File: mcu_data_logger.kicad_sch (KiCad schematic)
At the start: 0 parts

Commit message: second commit, dropped in components
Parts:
- added BT1: Battery, symbol Device:Battery
- added C1, C2, C3, C4: C, symbol Device:C
- added C5: C_Polarized, symbol Device:C_Polarized
- added D1, D2: LED, symbol Device:LED
- added H1, H2, H3, H4: MountingHole, symbol Mechanical:MountingHole
- added R1, R2, R3, R4, R5, R6, R7: R, symbol Device:R
- added U1, U2: 24LC1025, symbol Memory_EEPROM:24LC1025
- added U3: DS1337S_, DS1337S_:SOIC127P600X175-8N, symbol DS1337S_:DS1337S_
- added U4: ATMEGA328P-AU, ATMEGA328P-AU:QFP80P900X900X120-32N, symbol ATMEGA328P-AU:ATMEGA328P-AU
- added Y1, Y2: Crystal, symbol Device:Crystal
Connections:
- new net: U4.21 (GND), U4.3 (GND), U4.5 (GND)
- new net: U4.4 (VCC), U4.6 (VCC)

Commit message: arranged symbols on the schematic
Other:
- added sheet Connectors (connectors.kicad_sch)
- moved on the sheet: BT1, C1, C2, C3, C4, C5, D1, D2, R1, R2, R3, R4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

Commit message: assigned values to components
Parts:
- C1, C4: value C -> 0.1uF
- C2, C3: value C -> 22pF
- C5: value C_Polarized -> 100nF
- R1, R2, R6: value R -> 10k
- R3, R4: value R -> 4.7k
- R5, R7: value R -> 330
- Y1: value Crystal -> 32.768 kHz
- Y2: value Crystal -> 16MHz
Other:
- moved on the sheet: R7
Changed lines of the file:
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@@
 			)
 		)
-		(property "Value" "C"
+		(property "Value" "0.1uF"
 			(at 189.23 24.13 90)
 			(effects
@@
 			)
 		)
+		(property "Purpose" ""
+			(at 189.23 29.21 0)
+			(effects
+				(font
+					(size 1.27 1.27)
+				)
+			)
+		)
 		(pin "1"
 		)
@@
 			)
 		)
-		(property "Value" "C"
+		(property "Value" "0.1uF"
 			(at 134.62 52.0699 0)
 			(effects
@@
 			)
 		)
+		(property "Purpose" ""
+			(at 130.81 50.8 0)
+			(effects
+				(font
+					(size 1.27 1.27)
+				)
+			)
+		)
 		(pin "1"
 		)
@@
 			)
 		)
-		(property "Value" "C"
+		(property "Value" "22pF"
 			(at 177.8 77.4699 0)
 			(effects
@@
 			)
 		)
+		(property "Purpose" ""
+			(at 173.99 76.2 0)
+			(effects
+				(font
+					(size 1.27 1.27)
+				)
+			)
+		)
 		(pin "1"
 		)
@@
 			)
 		)
-		(property "Value" "C_Polarized"
+		(property "Value" "100nF"
 			(at 257.81 44.8309 0)
 			(effects
@@
 			)
 		)
+		(property "Purpose" ""
+			(at 254 44.45 0)
+			(effects
+				(font
+					(size 1.27 1.27)
+				)
+			)
+		)
 		(pin "1"
 		)
@@
 	(symbol
 		(lib_id "Device:R")
-		(at 256.54 82.55 0)
+		(at 254 76.2 0)
 		(unit 1)
 		(exclude_from_sim no)
@@
 		(fields_autoplaced yes)
 		(property "Reference" "R7"
-			(at 259.08 81.2799 0)
-			(effects
-				(font
-					(size 1.27 1.27)
-				)
-				(justify left)
-			)
-		)
-		(property "Value" "R"
-			(at 259.08 83.8199 0)
-			(effects
-				(font
-					(size 1.27 1.27)
-				)
-				(justify left)
-			)
-		)
-		(property "Footprint" ""
-			(at 254.762 82.55 90)
+			(at 256.54 74.9299 0)
+			(effects
+				(font
+					(size 1.27 1.27)
+				)
+				(justify left)
+			)
+		)
+		(property "Value" "330"
+			(at 256.54 77.4699 0)
+			(effects
+				(font
+					(size 1.27 1.27)
+				)
+				(justify left)
+			)
+		)
+		(property "Footprint" ""
+			(at 252.222 76.2 90)
 			(effects
 				(font
@@
 		)
 		(property "Datasheet" "~"
-			(at 256.54 82.55 0)
+			(at 254 76.2 0)
 			(effects
 				(font
@@
 		)
 		(property "Description" "Resistor"
-			(at 256.54 82.55 0)
-			(effects
-				(font
-					(size 1.27 1.27)
-				)
-				(hide yes)
+			(at 254 76.2 0)
+			(effects
+				(font
+					(size 1.27 1.27)
+				)
+				(hide yes)
+			)
+		)
+		(property "Purpose" ""
+			(at 254 76.2 0)
+			(effects
+				(font
+					(size 1.27 1.27)
+				)
 			)
 		)
@@
 				(path "/8d241645-05dd-4180-8806-a9efe0716d11"
 					(reference "R7")
+					(unit 1)
+				)
+			)
+		)
+	)
+	(symbol
+		(lib_id "Device:R")
+		(at 130.81 172.72 0)
+		(unit 1)
+		(exclude_from_sim no)
+		(in_bom yes)
+		(on_board yes)
+		(dnp no)
+		(fields_autoplaced yes)
+		(property "Reference" "R3"
+			(at 133.35 171.4499 0)
+			(effects
+				(font
+					(size 1.27 1.27)
+				)
+				(justify left)
+			)
+		)
+		(property "Value" "4.7k"
+			(at 133.35 173.9899 0)
+			(effects
+				(font
+					(size 1.27 1.27)
+				)
+				(justify left)
+			)
+		)
+		(property "Footprint" ""
+			(at 129.032 172.72 90)
+			(effects
+				(font
+					(size 1.27 1.27)
+				)
+				(hide yes)
+			)
+		)
+		(property "Datasheet" "~"
+			(at 130.81 172.72 0)
+			(effects
+				(font
+					(size 1.27 1.27)
+				)
+				(hide yes)
+			)
+		)
+		(property "Description" "Resistor"
+			(at 130.81 172.72 0)
+			(effects
+				(font
+					(size 1.27 1.27)
+				)
+				(hide yes)
+			)
+		)
+		(property "Purpose" ""
+			(at 130.81 172.72 0)
+			(effects
+				(font
+					(size 1.27 1.27)
+				)
+			)
+		)
+		(pin "1"
+		)
+		(pin "2"
+		)
+		(instances
+			(project "mcu_data_logger"
+				(path "/8d241645-05dd-4180-8806-a9efe0716d11"
+					(reference "R3")
 					(unit 1)
 				)
@@
 			)
 		)
-		(property "Value" "R"
+		(property "Value" "10k"
 			(at 109.22 52.0699 0)
 			(effects
@@
 			)
 		)
+		(property "Purpose" ""
+			(at 106.68 50.8 0)
+			(effects
+				(font
+					(size 1.27 1.27)
+				)
+			)
+		)
 		(pin "1"
 		)
@@
 			)
 		)
-		(property "Value" "R"
+		(property "Value" "330"
 			(at 173.99 41.91 90)
 			(effects
@@
 			)
 		)
+		(property "Purpose" ""
+			(at 173.99 45.72 0)
+			(effects
+				(font
+					(size 1.27 1.27)
+				)
+			)
+		)
 		(pin "1"
 		)
@@
 			)
 		)
-		(property "Value" "R"
+		(property "Value" "10k"
 			(at 120.65 52.0699 0)
 			(effects
@@
 			)
 		)
+		(property "Purpose" ""
+			(at 118.11 50.8 0)
+			(effects
+				(font
+					(size 1.27 1.27)
+				)
+			)
+		)
 		(pin "1"
 		)
@@
 			)
 		)
-		(property "Value" "Crystal"
+		(property "Value" "32.768 kHz"
 			(at 48.26 52.0699 90)
 			(effects
@@
 			)
 		)
-		(property "Value" "C"
+		(property "Value" "22pF"
 			(at 177.8 59.6899 0)
 			(effects
@@
 			)
 		)
+		(property "Purpose" ""
+			(at 173.99 58.42 0)
+			(effects
+				(font
+					(size 1.27 1.27)
+				)
+			)
+		)
 		(pin "1"
 		)
@@
 				(path "/8d241645-05dd-4180-8806-a9efe0716d11"
 					(reference "C2")
-					(unit 1)
-				)
-			)
-		)
-	)
-	(symbol
-		(lib_id "Device:R")
-		(at 132.08 172.72 180)
-		(unit 1)
-		(exclude_from_sim no)
-		(in_bom yes)
-		(on_board yes)
-		(dnp no)
-		(fields_autoplaced yes)
-		(property "Reference" "R3"
-			(at 134.62 171.4499 0)
-			(effects
-				(font
-					(size 1.27 1.27)
-				)
-				(justify right)
-			)
-		)
-		(property "Value" "R"
-			(at 134.62 173.9899 0)
-			(effects
-				(font
-					(size 1.27 1.27)
-				)
-				(justify right)
-			)
-		)
-		(property "Footprint" ""
-			(at 133.858 172.72 90)
-			(effects
-				(font
-					(size 1.27 1.27)
-				)
-				(hide yes)
-			)
-		)
-		(property "Datasheet" "~"
-			(at 132.08 172.72 0)
-			(effects
-				(font
-					(size 1.27 1.27)
-				)
-				(hide yes)
-			)
-		)
-		(property "Description" "Resistor"
-			(at 132.08 172.72 0)
-			(effects
-				(font
-					(size 1.27 1.27)
-				)
-				(hide yes)
-			)
-		)
-		(pin "1"
-		)
-		(pin "2"
-		)
-		(instances
-			(project "mcu_data_logger"
-				(path "/8d241645-05dd-4180-8806-a9efe0716d11"
-					(reference "R3")
 					(unit 1)
 				)
@@
 			)
 		)
-		(property "Value" "R"
+		(property "Value" "10k"
 			(at 198.12 81.28 90)
 			(effects
@@
 			)
 		)
+		(property "Purpose" ""
+			(at 198.12 85.09 0)
+			(effects
+				(font
+					(size 1.27 1.27)
+				)
+			)
+		)
 		(pin "1"
 		)
@@
 			)
 		)
-		(property "Value" "Crystal"
+		(property "Value" "16MHz"
 			(at 194.31 63.4999 90)
 			(effects
@@
 			)
 		)
+		(property "Purpose" ""
+			(at 190.5 62.23 0)
+			(effects
+				(font
+					(size 1.27 1.27)
+				)
+			)
+		)
 		(pin "2"
 		)
@@
 			)
 		)
-		(property "Value" "R"
+		(property "Value" "4.7k"
 			(at 143.51 173.9899 0)
 			(effects
@@
 			)
 		)
+		(property "Purpose" ""
+			(at 140.97 172.72 0)
+			(effects
+				(font
+					(size 1.27 1.27)
+				)
+			)
+		)

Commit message: assigned footprints and added libraries
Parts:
- BT1: footprint (none) -> Connector_PinHeader_2.54mm:PinHeader_1x02_P2.54mm_Horizontal
- C1, C2, C3, C4, C5: footprint (none) -> Capacitor_SMD:C_0805_2012Metric
- D1, D2: footprint (none) -> LED_SMD:LED_0805_2012Metric
- H1, H2, H3, H4: footprint (none) -> MountingHole:MountingHole_2.1mm
- R1, R2, R3, R4, R5, R6, R7: footprint (none) -> Resistor_SMD:R_0805_2012Metric
- U1, U2: footprint (none) -> Package_SO:SOIC-8_5.3x5.3mm_P1.27mm
- U3: footprint DS1337S_:SOIC127P600X175-8N -> footprints:SOIC127P600X175-8N
- U4: footprint ATMEGA328P-AU:QFP80P900X900X120-32N -> footprints:QFP80P900X900X120-32N
- Y1, Y2: footprint (none) -> Crystal:Crystal_SMD_5032-2Pin_5.0x3.2mm_HandSoldering
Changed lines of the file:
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@@
 			)
 		)
-		(property "Footprint" ""
+		(property "Footprint" "Capacitor_SMD:C_0805_2012Metric"
 			(at 193.04 28.2448 0)
 			(effects
@@
 			)
 		)
-		(property "Footprint" ""
+		(property "Footprint" "Capacitor_SMD:C_0805_2012Metric"
 			(at 131.7752 54.61 0)
 			(effects
@@
 			)
 		)
-		(property "Footprint" ""
+		(property "Footprint" "Capacitor_SMD:C_0805_2012Metric"
 			(at 174.9552 80.01 0)
 			(effects
@@
 			)
 		)
-		(property "Footprint" ""
+		(property "Footprint" "Capacitor_SMD:C_0805_2012Metric"
 			(at 254.9652 48.26 0)
 			(effects
@@
 			)
 		)
-		(property "Footprint" ""
+		(property "Footprint" "Connector_PinHeader_2.54mm:PinHeader_1x02_P2.54mm_Horizontal"
 			(at 267.97 42.926 90)
 			(effects
@@
 			)
 		)
-		(property "Footprint" ""
+		(property "Footprint" "MountingHole:MountingHole_2.1mm"
 			(at 200.66 151.13 0)
 			(effects
@@
 			)
 		)
-		(property "Footprint" ""
+		(property "Footprint" "Package_SO:SOIC-8_5.3x5.3mm_P1.27mm"
 			(at 110.49 172.72 0)
 			(effects
@@
 			)
 		)
-		(property "Footprint" ""
+		(property "Footprint" "Package_SO:SOIC-8_5.3x5.3mm_P1.27mm"
 			(at 80.01 172.72 0)
 			(effects
@@
 			)
 		)
-		(property "Footprint" ""
+		(property "Footprint" "Resistor_SMD:R_0805_2012Metric"
 			(at 252.222 76.2 90)
 			(effects
@@
 			)
 		)
-		(property "Footprint" ""
+		(property "Footprint" "Resistor_SMD:R_0805_2012Metric"
 			(at 129.032 172.72 90)
 			(effects
@@
 			)
 		)
-		(property "Footprint" ""
+		(property "Footprint" "LED_SMD:LED_0805_2012Metric"
 			(at 189.23 45.72 0)
 			(effects
@@
 			)
 		)
-		(property "Footprint" ""
+		(property "Footprint" "Resistor_SMD:R_0805_2012Metric"
 			(at 104.902 50.8 90)
 			(effects
@@
 			)
 		)
-		(property "Footprint" ""
+		(property "Footprint" "MountingHole:MountingHole_2.1mm"
 			(at 200.66 140.97 0)
 			(effects
@@
 			)
 		)
-		(property "Footprint" ""
+		(property "Footprint" "Resistor_SMD:R_0805_2012Metric"
 			(at 173.99 47.498 90)
 			(effects
@@
 			)
 		)
-		(property "Footprint" ""
+		(property "Footprint" "Resistor_SMD:R_0805_2012Metric"
 			(at 116.332 50.8 90)
 			(effects
@@
 			)
 		)
-		(property "Footprint" "DS1337S_:SOIC127P600X175-8N"
+		(property "Footprint" "footprints:SOIC127P600X175-8N"
 			(at 73.66 53.34 0)
 			(effects
@@
 			)
 		)
-		(property "Footprint" ""
+		(property "Footprint" "Crystal:Crystal_SMD_5032-2Pin_5.0x3.2mm_HandSoldering"
 			(at 44.45 50.8 0)
 			(effects
@@
 			)
 		)
-		(property "Footprint" ""
+		(property "Footprint" "LED_SMD:LED_0805_2012Metric"
 			(at 254 62.23 0)
 			(effects
@@
 			)
 		)
-		(property "Footprint" ""
+		(property "Footprint" "Capacitor_SMD:C_0805_2012Metric"
 			(at 174.9552 62.23 0)
 			(effects
@@
 			)
 		)
-		(property "Footprint" ""
+		(property "Footprint" "Resistor_SMD:R_0805_2012Metric"
 			(at 198.12 86.868 90)
 			(effects
@@
 			)
 		)
-		(property "Footprint" ""
+		(property "Footprint" "MountingHole:MountingHole_2.1mm"
 			(at 200.66 128.27 0)
 			(effects
@@
 			)
 		)
-		(property "Footprint" "ATMEGA328P-AU:QFP80P900X900X120-32N"
+		(property "Footprint" "footprints:QFP80P900X900X120-32N"
 			(at 227.33 60.96 0)
 			(effects
@@
 			)
 		)
-		(property "Footprint" ""
+		(property "Footprint" "MountingHole:MountingHole_2.1mm"
 			(at 200.66 119.38 0)
 			(effects
@@
 			)
 		)
-		(property "Footprint" ""
+		(property "Footprint" "Crystal:Crystal_SMD_5032-2Pin_5.0x3.2mm_HandSoldering"
 			(at 190.5 62.23 0)
 			(effects
@@
 			)
 		)
-		(property "Footprint" ""
+		(property "Footprint" "Resistor_SMD:R_0805_2012Metric"
 			(at 139.192 172.72 90)
 			(effects

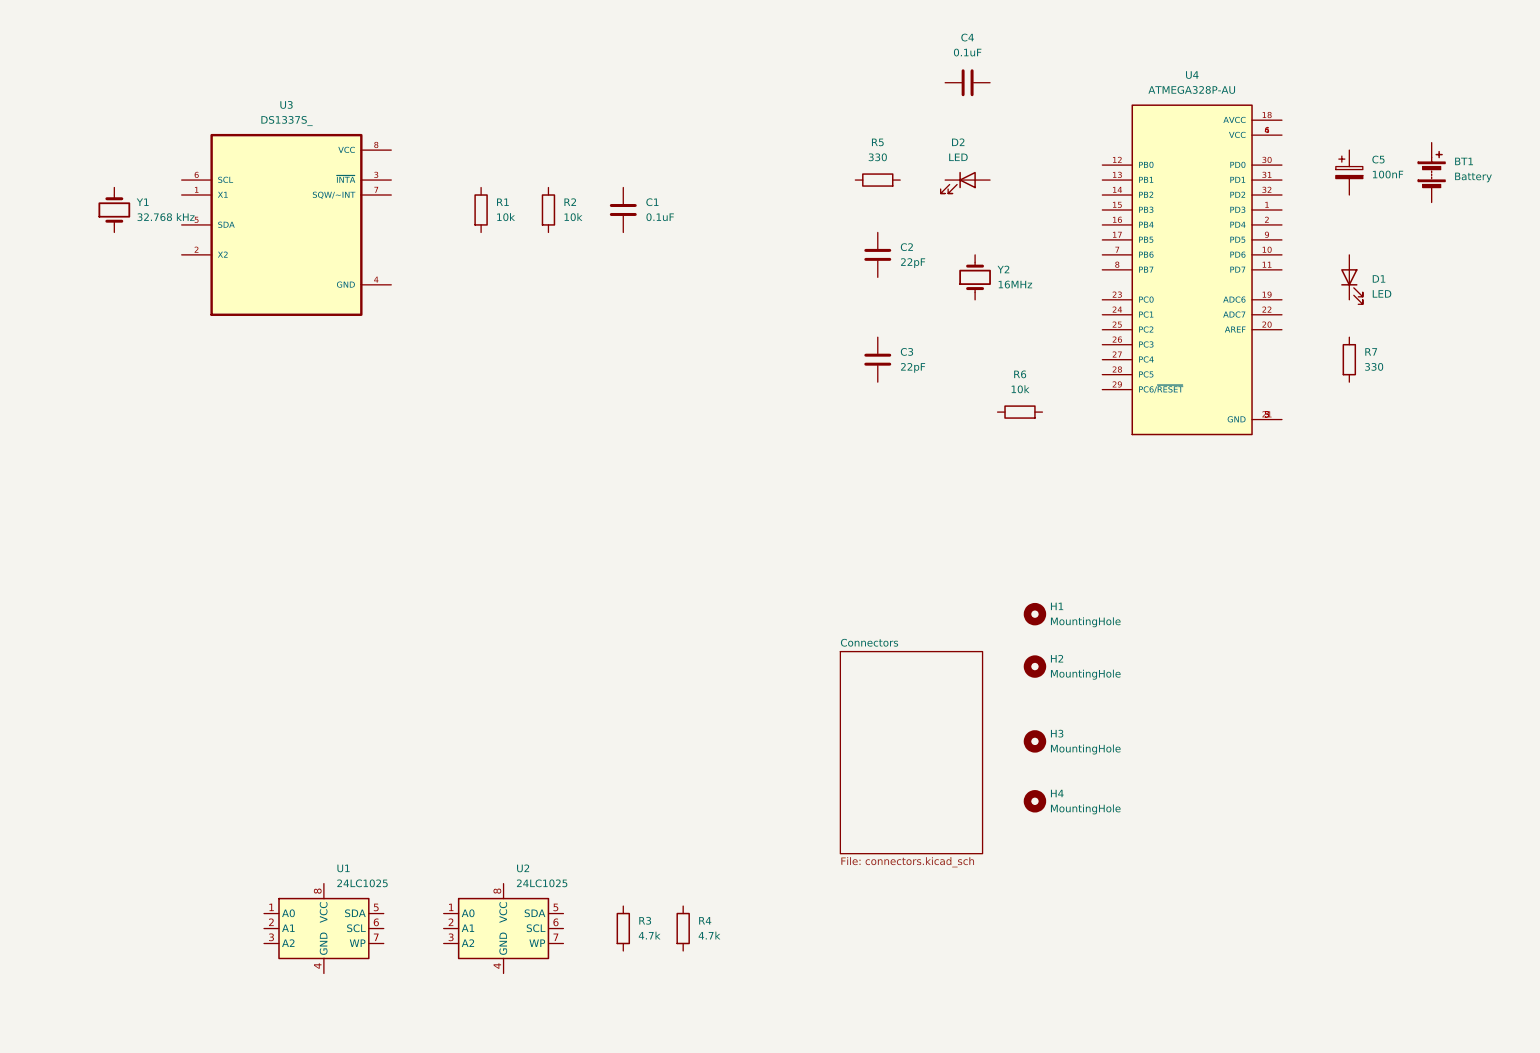
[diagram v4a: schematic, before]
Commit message: wiring for main sheet finished
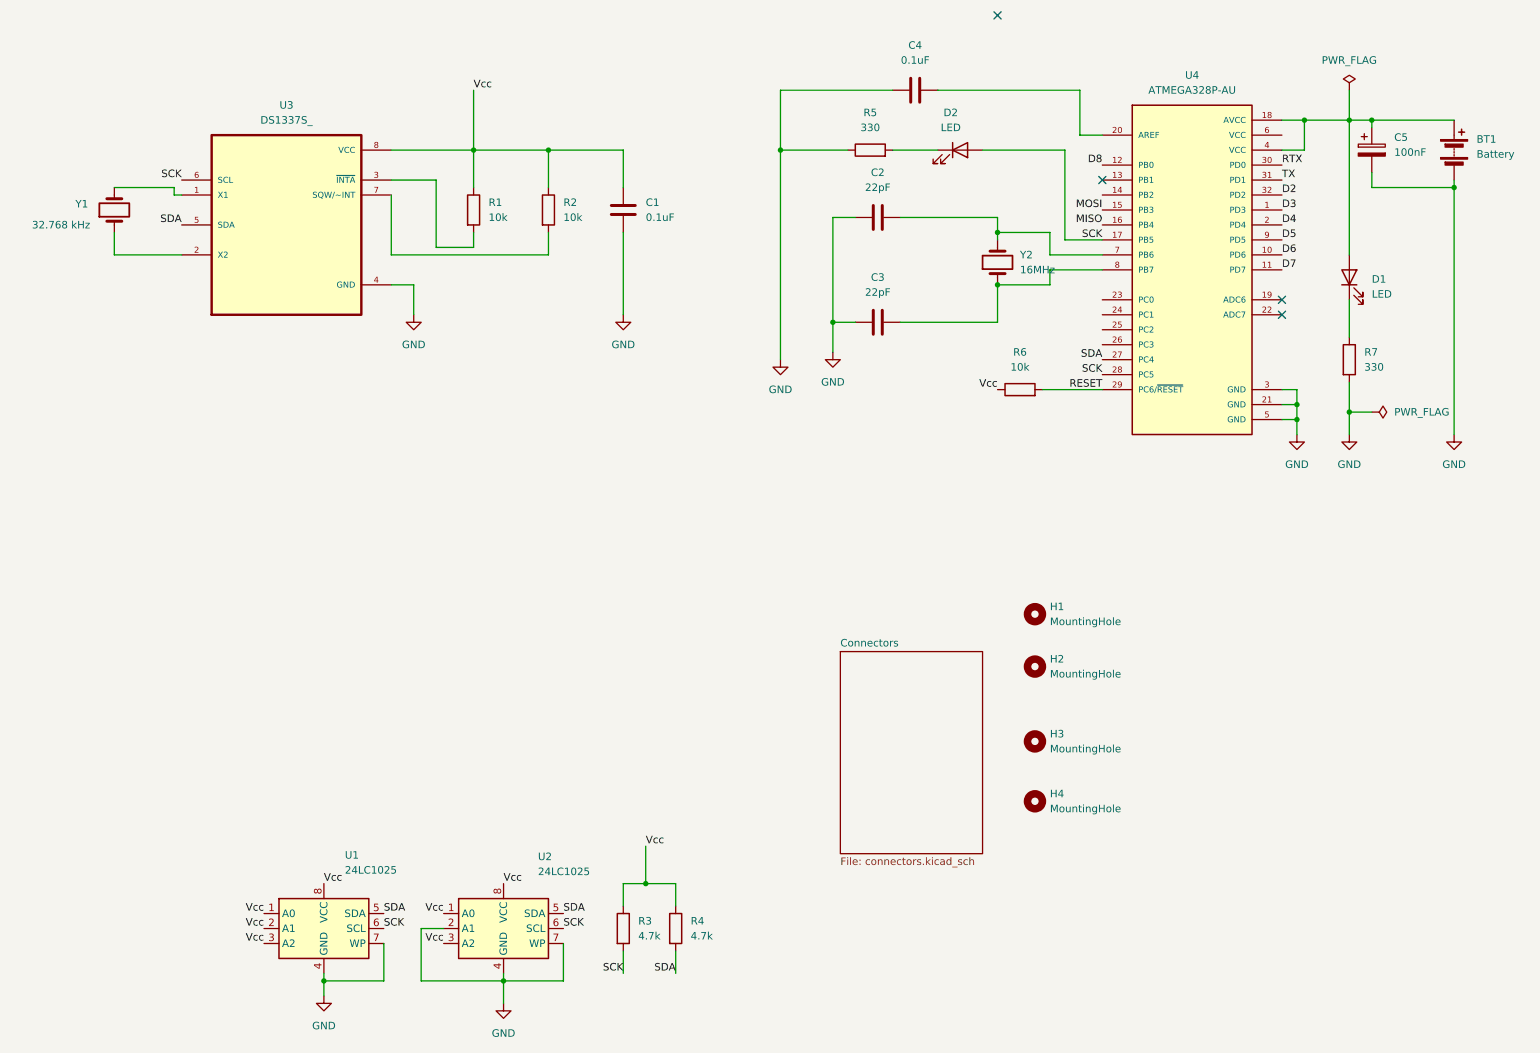
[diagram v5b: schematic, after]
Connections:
- net GND: now reaches C4.1
- net GND: now also BT1.2 (-), C1.2, C2.1, C3.1, C5.2, R5.1, R7.2, U1.4 (GND), U1.7 (WP), U2.2 (A1), U2.4 (GND), U2.7 (WP), U3.4 (GND), U4.21 (GND), U4.3 (GND), U4.5 (GND)
- net at C4.2: now also U4.20 (AREF)
- net Vcc: now reaches C1.1
- net Vcc: now also R1.1, R2.1, R3.1, R4.1, R6.1, U1.1 (A0), U1.2 (A1), U1.3 (A2), U1.8 (VCC), U2.1 (A0), U2.3 (A2), U2.8 (VCC), U3.8 (VCC)
- net at C3.2: now also U4.8 (PB7), Y2.1
- net at C5.1: now also BT1.1 (+), D1.2 (A), U4.18 (AVCC), U4.4 (VCC)
- net SDA: now reaches U2.5 (SDA)
- net SDA: now also R4.2, U1.5 (SDA), U3.5 (SDA), U4.27 (PC4)
- net SCK: now reaches U2.6 (SCL)
- net SCK: now also D2.2 (A), R3.2, U1.6 (SCL), U3.6 (SCL), U4.17 (PB5), U4.28 (PC5)
- net at R7.1: now also D1.1 (K)
- net at D2.1 (K): now also R5.2
- net at R1.2: now also U3.3 (~{INTA})
- net at R2.2: now also U3.7 (SQW/~INT)
- net at U3.1 (X1): now also Y1.2
- net at U3.2 (X2): now also Y1.1
- net at C2.2: now also U4.7 (PB6), Y2.2
- net RESET: now reaches R6.2
- net RESET: now also U4.29 (PC6/~{RESET})
- net D3: now reaches U4.1 (PD3)
- net D6: now reaches U4.10 (PD6)
- net D7: now reaches U4.11 (PD7)
- net D8: now reaches U4.12 (PB0)
- net MOSI: now reaches U4.15 (PB3)
- net MISO: now reaches U4.16 (PB4)
- net D4: now reaches U4.2 (PD4)
- net RTX: now reaches U4.30 (PD0)
- net TX: now reaches U4.31 (PD1)
- net D2: now reaches U4.32 (PD2)
- net at U4.6 (VCC): no longer U4.4 (VCC)
- net D5: now reaches U4.9 (PD5)
- no-connect marks 0 -> 4
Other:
- moved on the sheet: BT1, C2, C3, C4, C5, D2, R1, R4, R5, R6, Y2
